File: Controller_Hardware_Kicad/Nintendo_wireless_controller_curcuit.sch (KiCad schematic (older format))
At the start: 24 parts, among them IC1 ATTINY24-SS, J1 BATT, J2 NRF_conn, P1 CONN_1, U1 MAX1811, U2 LP5951MF-3.3, X1 USB-MB-S, X2 8MHz, sw1 CONN_2

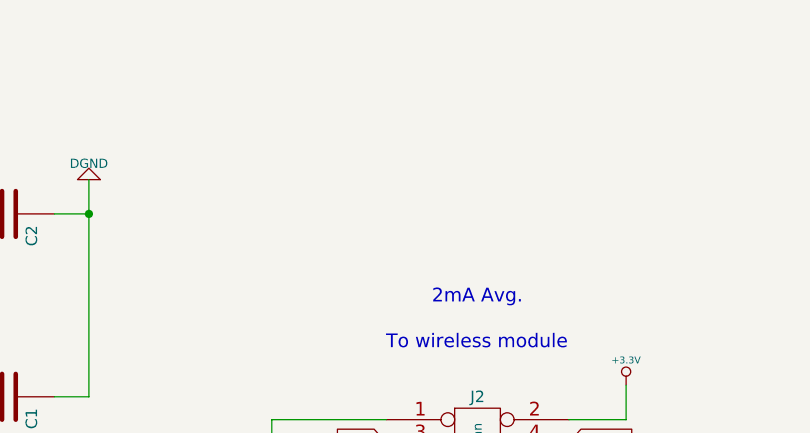
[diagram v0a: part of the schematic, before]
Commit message: added voltage divider.. havent calibrated yet.. also debugwire pinhole is wrong
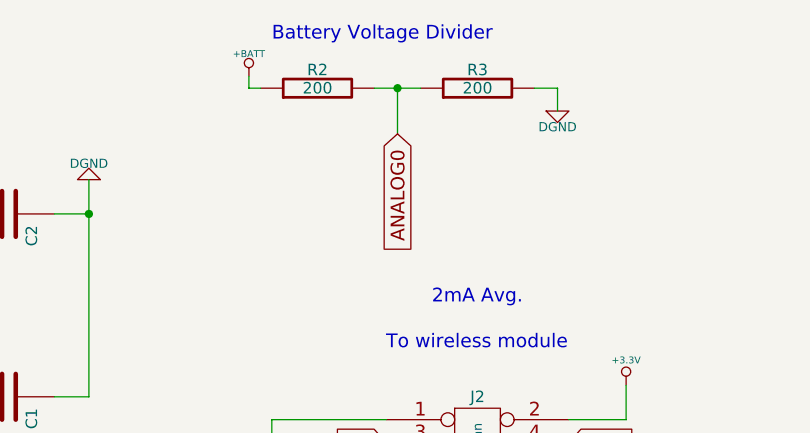
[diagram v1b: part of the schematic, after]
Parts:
- added R2, R3: 200, symbol R
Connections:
- net +BATT: now also R2.1
- net ANALOG0: now also R2.2, R3.1
- net DGND: now also R3.2
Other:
- note added: "Battery Voltage Divider"

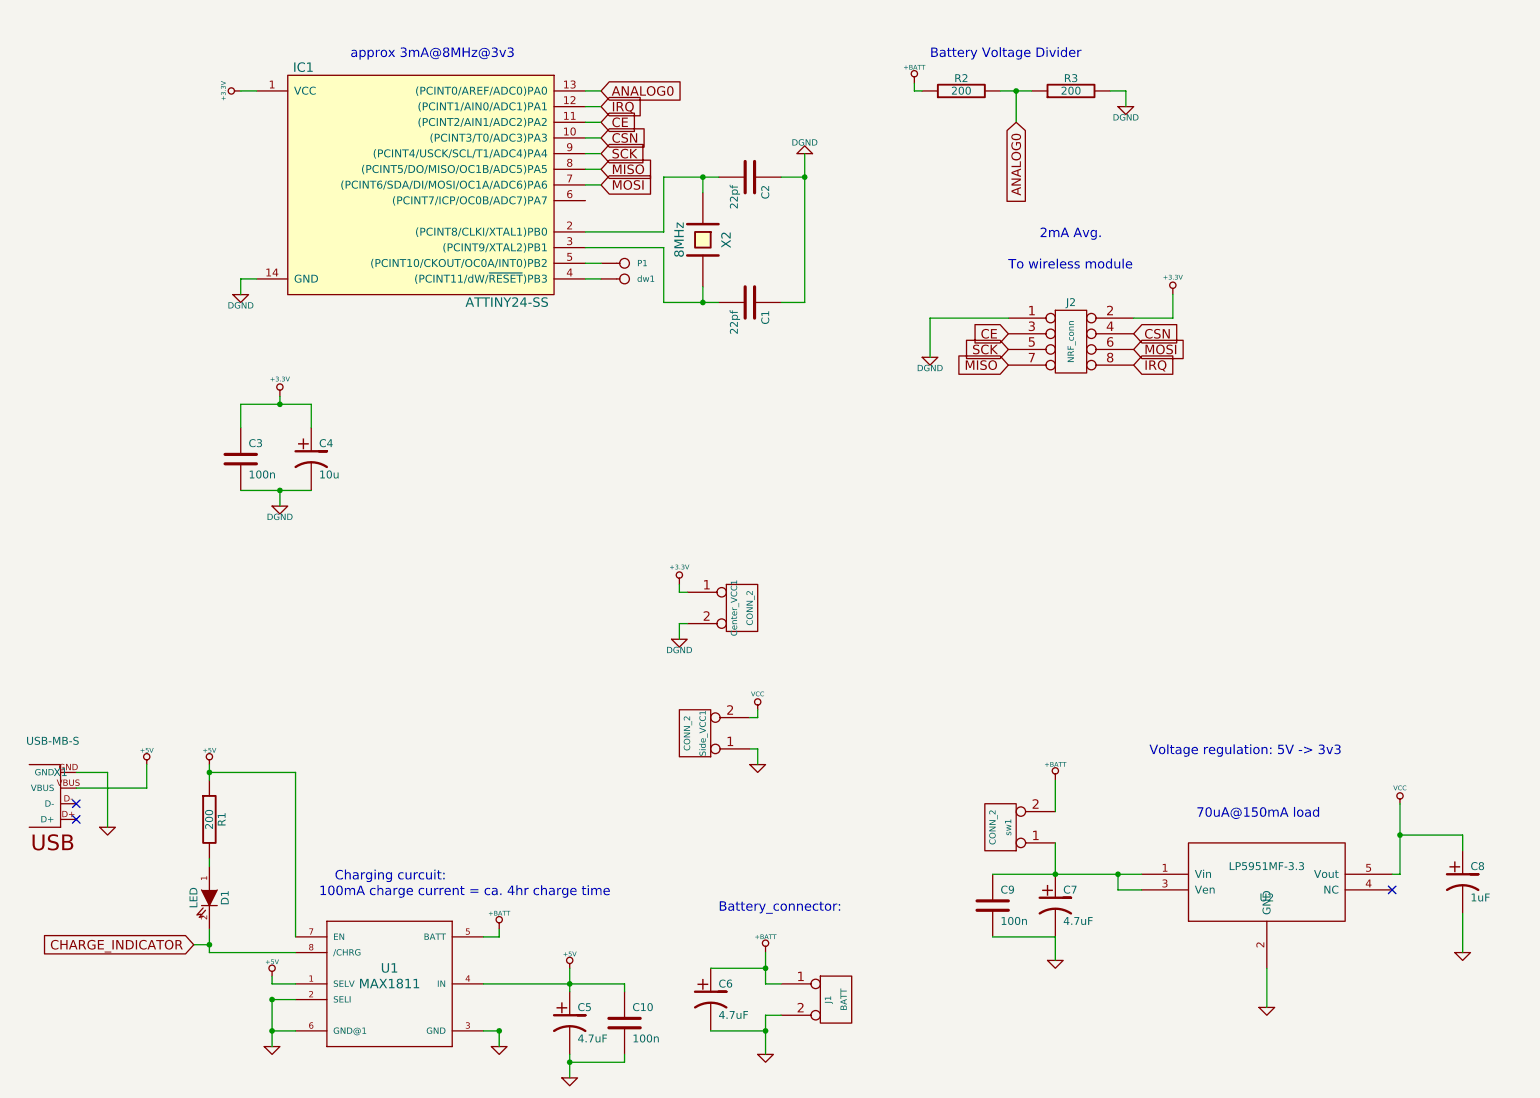
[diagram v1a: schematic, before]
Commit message: all footprints now proper. needs more routing.
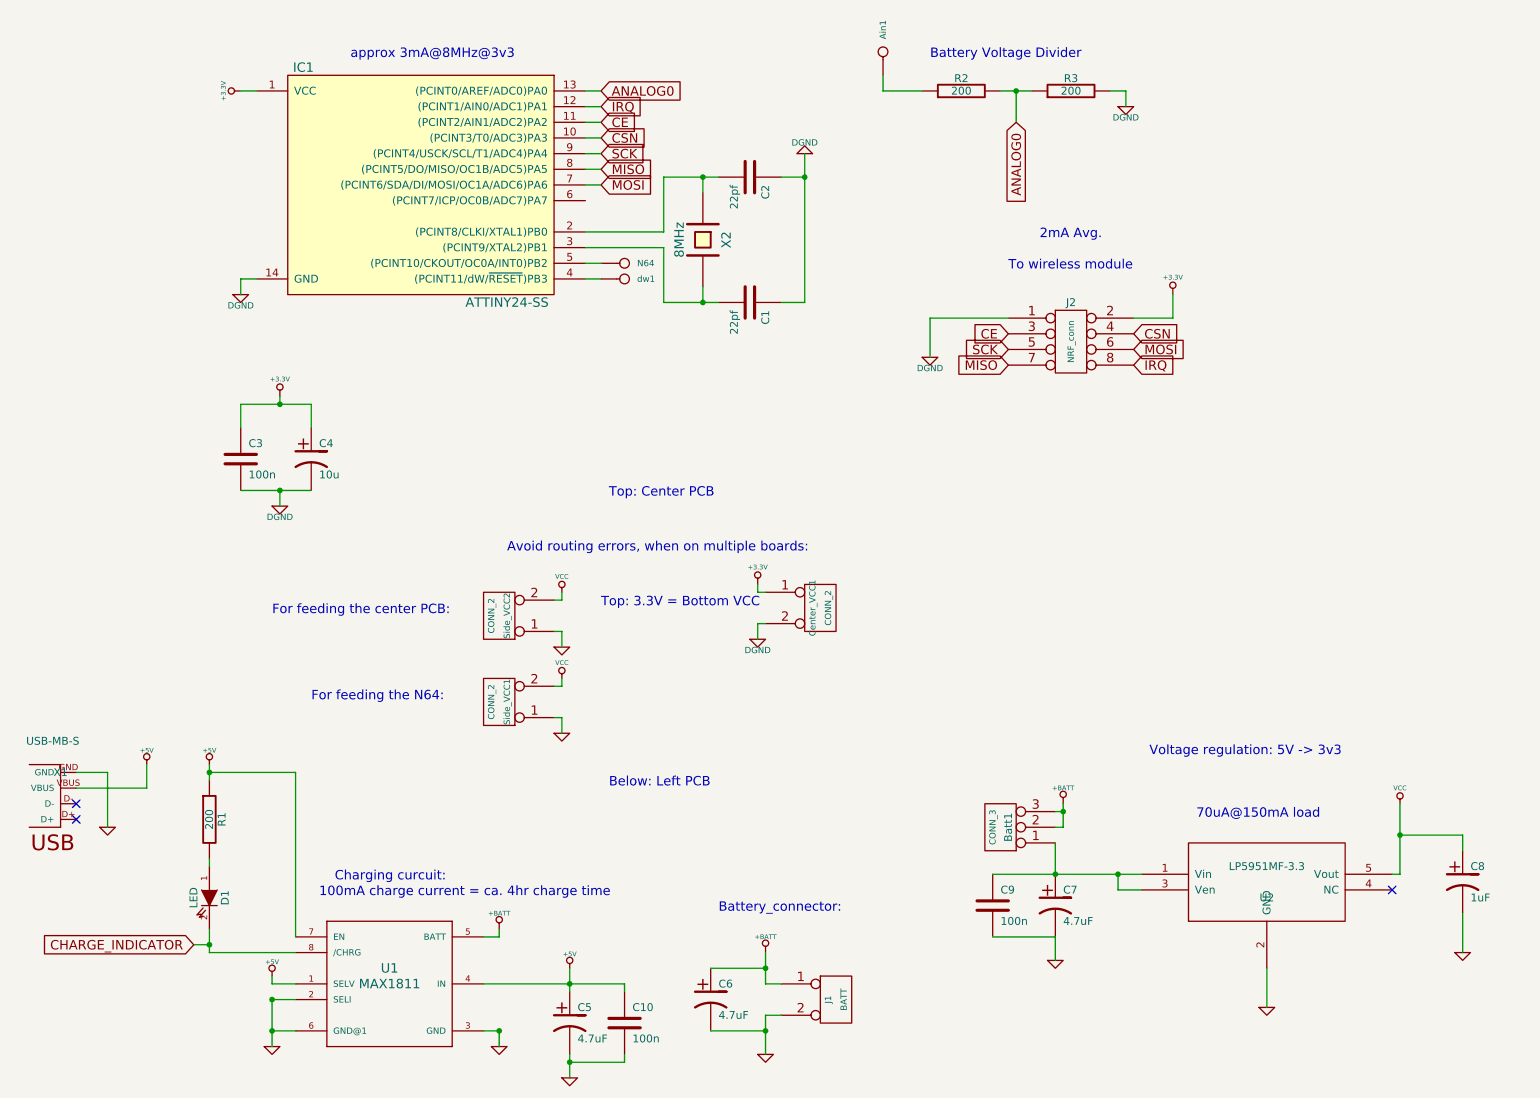
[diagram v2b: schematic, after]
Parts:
- removed sw1: CONN_2, symbol CONN_2
- added Ain1: CONN_1, symbol CONN_1
- added Batt1: CONN_3, symbol CONN_3
- added Side_VCC2: CONN_2, symbol CONN_2
- renumbered P1 to N64
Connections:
- net +BATT: now also Batt1.2 (PM), Batt1.3 (P3); no longer R2.1
- net GND: now also Side_VCC2.1 (P1)
- net VCC: now also Side_VCC2.2 (PM)
- net at C7.1, C9.1, U2.1 (Vin)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: now also Batt1.1 (P1)
- new net: Ain1.1, R2.1
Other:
- note added: "Avoid routing errors, when on multiple boards:"
- note added: "Below: Left PCB"
- note added: "For feeding the N64:"
- note added: "For feeding the center PCB:"
- note added: "Top: 3.3V = Bottom VCC"
- note added: "Top: Center PCB"
- moved on the sheet: Center_VCC1, Side_VCC1

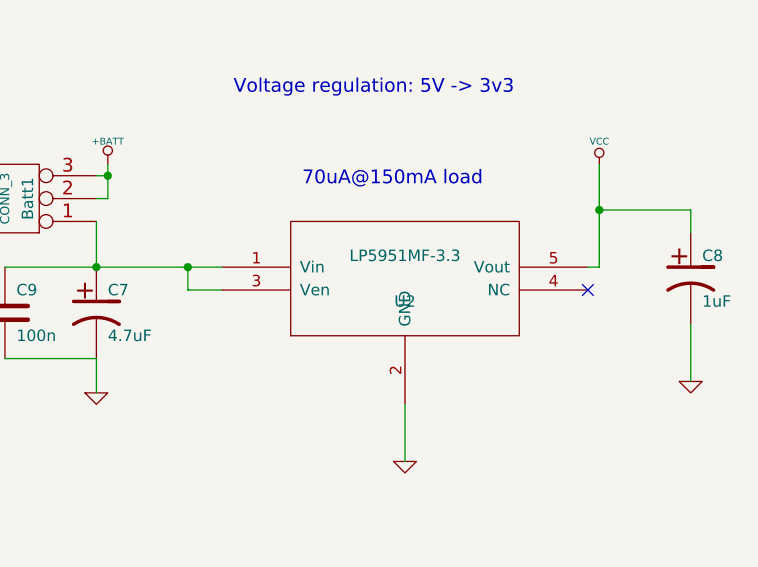
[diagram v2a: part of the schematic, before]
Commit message: starting to unfold the maxim1595 buck-boost instead of the LDO
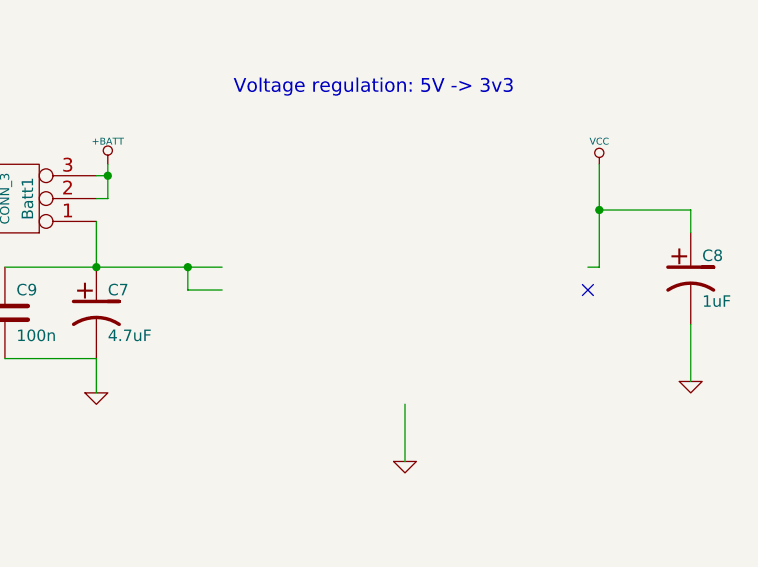
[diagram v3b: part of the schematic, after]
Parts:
- removed U2: LP5951MF-3.3, MODULE, symbol LP5951MF-3.3
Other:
- note removed: "70uA@150mA load"
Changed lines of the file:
@@
-EESchema Schematic File Version 2  date 24-06-2012 19:59:39
+EESchema Schematic File Version 2  date 26-06-2012 18:31:14
 LIBS:power
 LIBS:device
@@
 Sheet 1 1
 Title ""
-Date "24 jun 2012"
+Date "26 jun 2012"
 Rev ""
 Comp ""
@@
 Text Notes 7450 1950 0    60   ~ 0
 2mA Avg.
-Text Notes 8450 5650 0    60   ~ 0
-70uA@150mA load
 $Comp
 L CP1 C4
@@
 	1    0    0    -1
 $EndComp
-$Comp
-L LP5951MF-3.3 U2
-U 1 1 4F5F6802
-P 8900 6050
-F 0 "U2" H 8900 5950 50  0000 C CNN
-F 1 "LP5951MF-3.3" H 8900 6150 50  0000 C CNN
-F 2 "MODULE" H 8900 6050 50  0001 C CNN
-F 3 "DOCUMENTATION" H 8900 6050 50  0001 C CNN
-	1    8900 6050
-	1    0    0    -1
-$EndComp

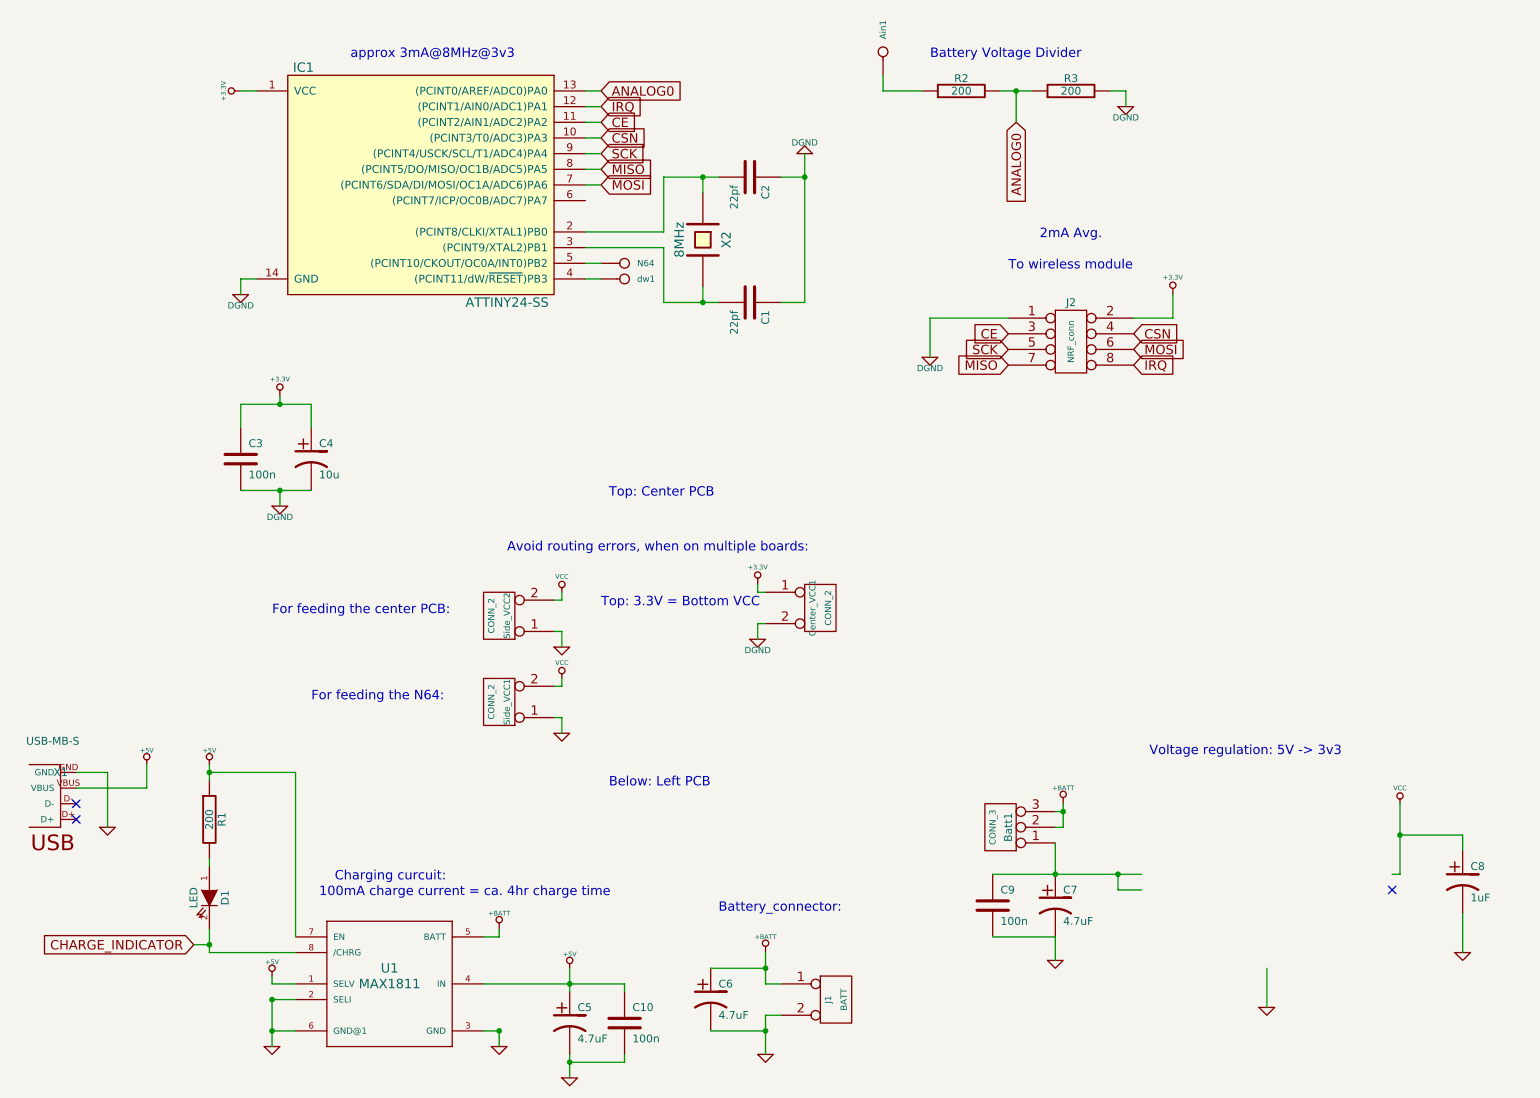
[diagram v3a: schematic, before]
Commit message: now with step-up step-down instead of LDO - not routed yet.
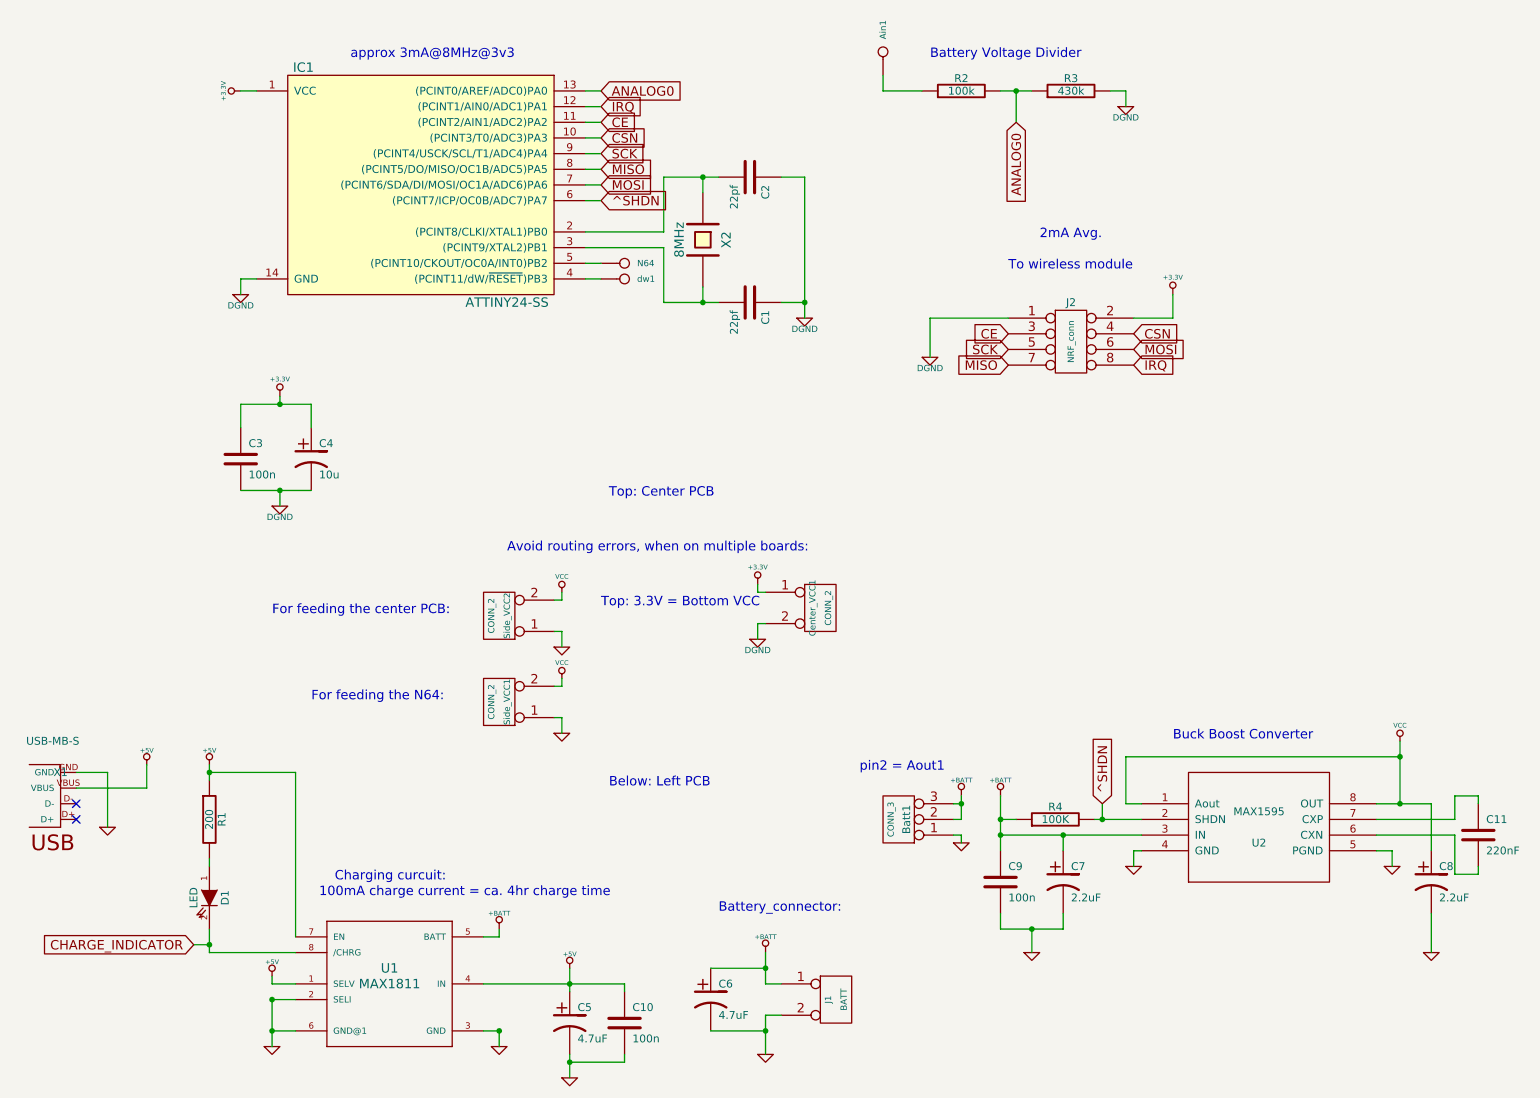
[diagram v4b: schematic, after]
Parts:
- added C11: 220nF, symbol C
- added R4: 100K, symbol R
- added U2: MAX1595, MODULE, symbol MAX1595
- C7: value 4.7uF -> 2.2uF
- C8: value 1uF -> 2.2uF
- R2: value 200 -> 100k
- R3: value 200 -> 430k
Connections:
- net labels added: ^SHDN
- wire segments 98 -> 118
- no-connect marks 3 -> 2
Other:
- note added: "Buck Boost Converter"
- note added: "pin2 = Aout1"
- note removed: "Voltage regulation: 5V -> 3v3\n"
- moved on the sheet: Batt1, C7, C8, C9
